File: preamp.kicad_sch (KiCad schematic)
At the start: 22 parts, among them U2 TL972QDRQ1

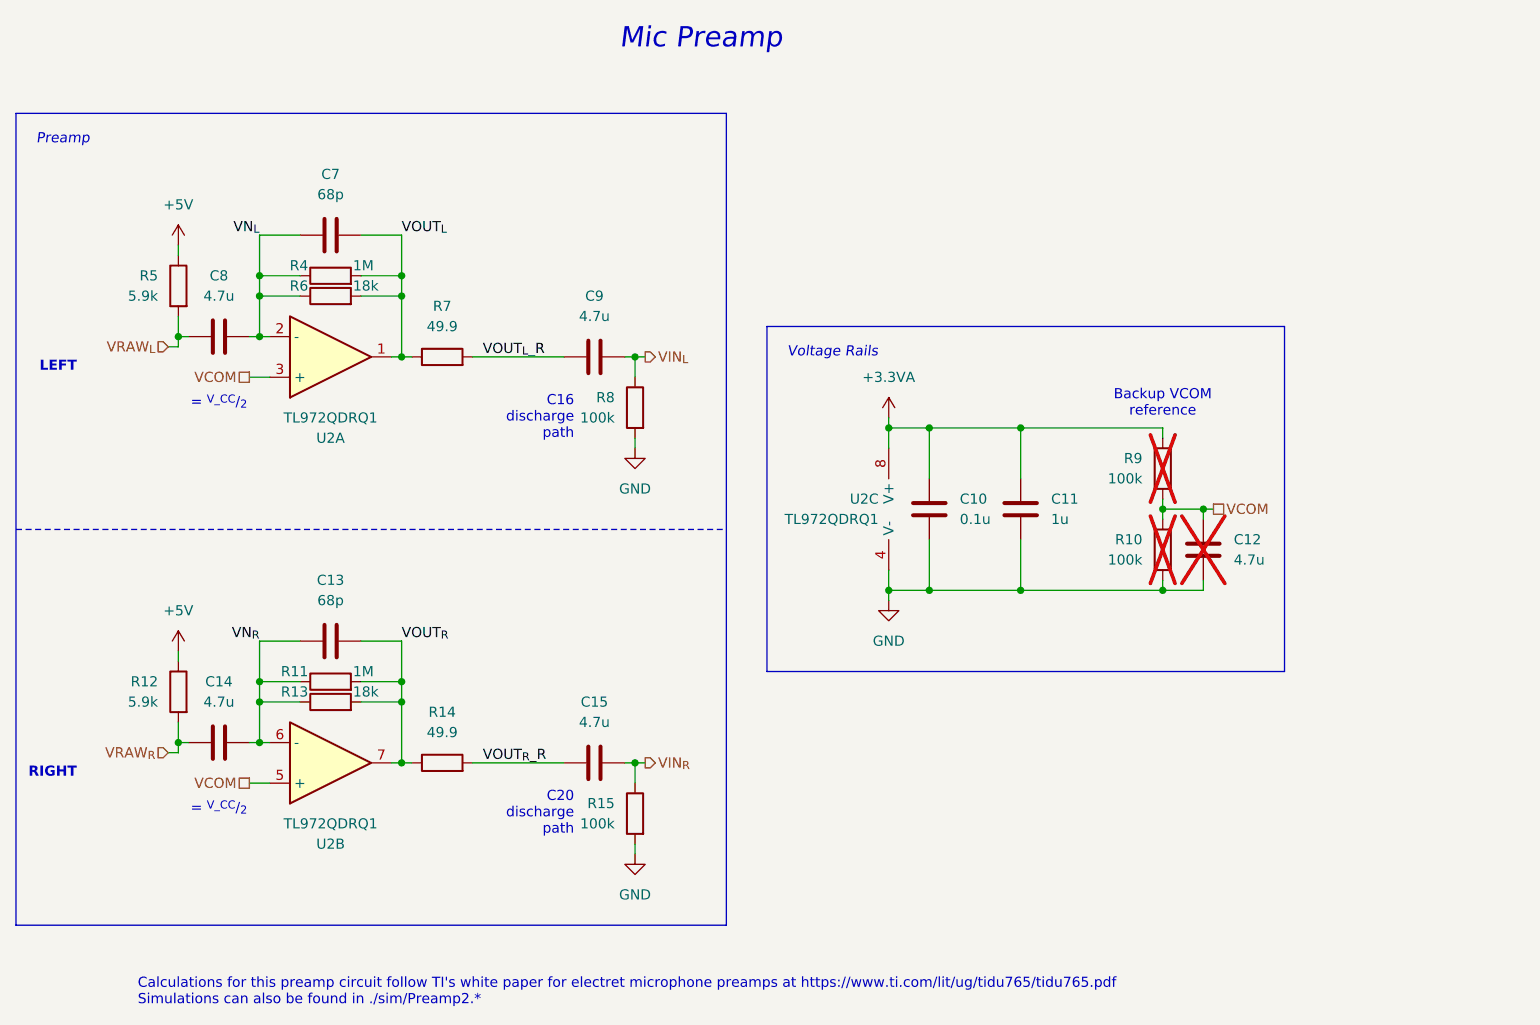
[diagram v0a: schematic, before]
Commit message: Redid schematic and component values according to new recalculations
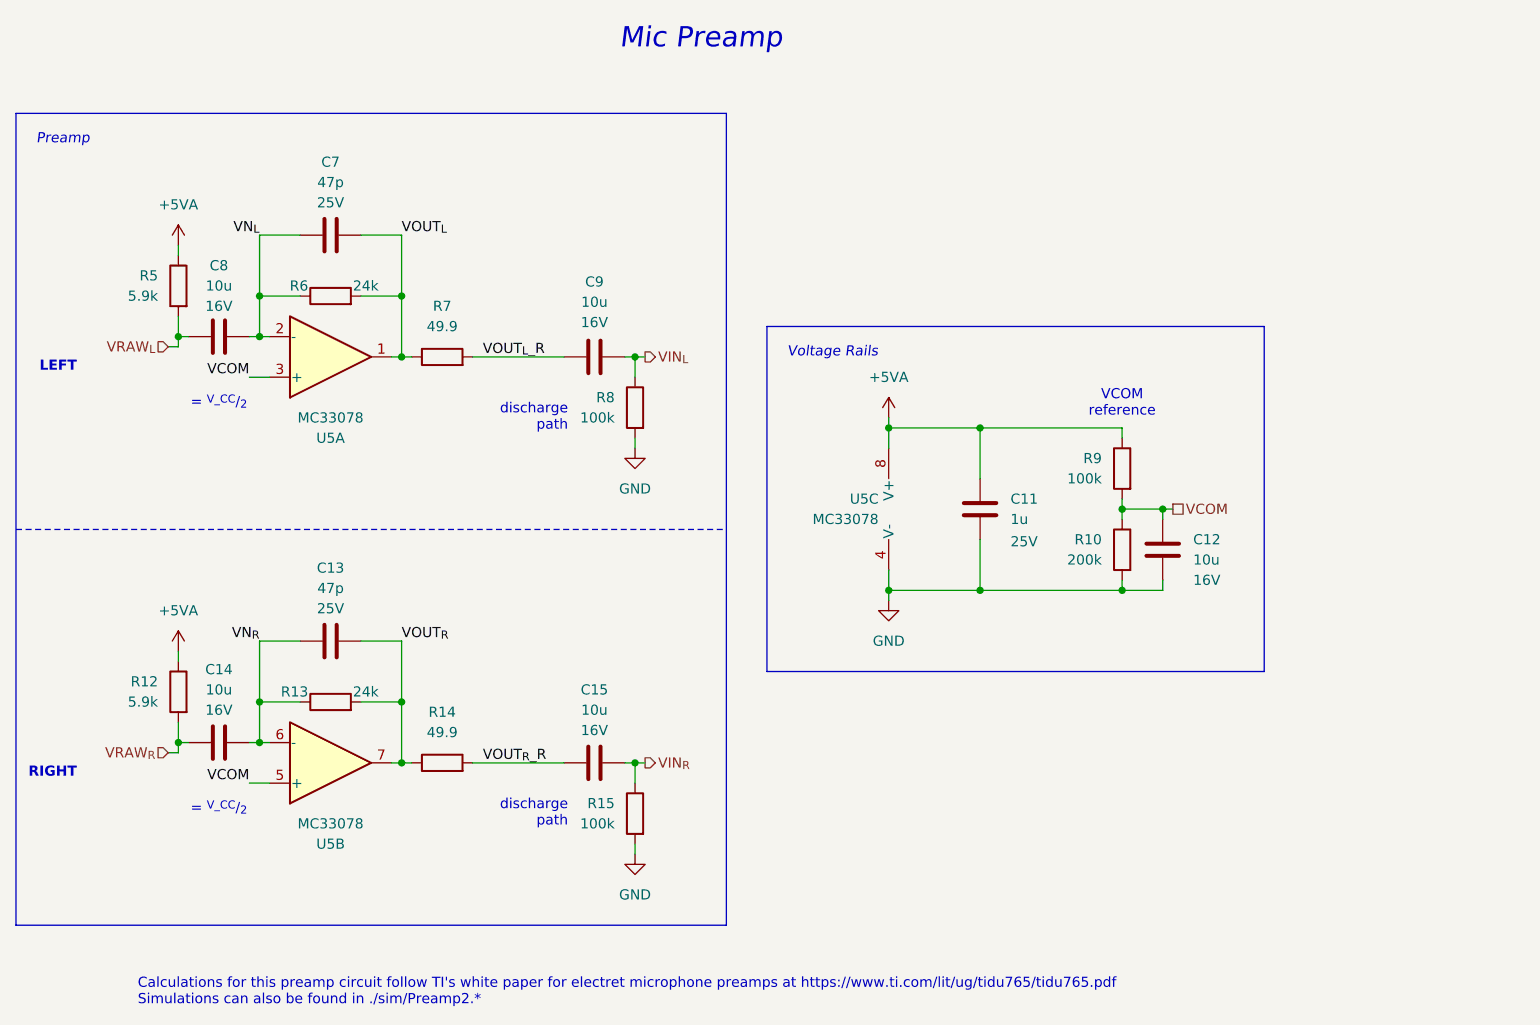
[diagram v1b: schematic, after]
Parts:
- removed C10: 0.1u, Capacitor_SMD:C_0805_2012Metric_Pad1.18x1.45mm_HandSolder, symbol Device:C
- removed R11, R4: 1M, Resistor_SMD:R_0603_1608Metric_Pad0.98x0.95mm_HandSolder, symbol Device:R
- removed U2: TL972QDRQ1, Package_SO:SOIC-8_3.9x4.9mm_P1.27mm, symbol Device:Opamp_Dual
- added U5: MC33078, Package_SO:SOIC-8_3.9x4.9mm_P1.27mm, symbol Amplifier_Operational:MC33078
- C11: footprint Capacitor_SMD:C_1206_3216Metric_Pad1.33x1.80mm_HandSolder -> Capacitor_SMD:C_0603_1608Metric_Pad1.08x0.95mm_HandSolder; Mouser Part Number 581-TAJA105K020TNJ -> 187-CL10B105KA8NNNL; Voltage Rating (none) -> 25V
- C12: value 4.7u -> 10u; Mouser Part Number 581-TAJA475K016R -> 581-TAJA106K016R; Voltage Rating (none) -> 16V; now fitted
- C13, C7: value 68p -> 47p; Mouser Part Number 77-VJ0603D680FXPAJ -> 77-VJ0603A470JXXCBC; Voltage Rating (none) -> 25V
- C14, C15, C8, C9: value 4.7u -> 10u; Mouser Part Number 581-TAJA475K016R -> 581-TAJA106K016R; Voltage Rating (none) -> 16V
- R10: value 100k -> 200k; Mouser Part Number 603-RT0603FRE10100KL -> 603-AF0603FR-07200KL; now fitted
- R13, R6: value 18k -> 24k; Mouser Part Number 667-ERA-3AEB183V -> 03-RT0603DRD0724KL
- R9: now fitted
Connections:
- net +5V is gone; now on net +5VA: R12.1, R5.1
- net GND: now also U5.4 (V-)
- net VCOM: now also U5.3 (+), U5.5 (+)
- net VN_{L}: now also U5.2 (-)
- net VN_{R}: now also U5.6 (-)
- net VOUT_{L}: now also U5.1
- net VOUT_{R}: now also U5.7
- net +3.3VA renamed +5VA
- net +5VA: now also U5.8 (V+)
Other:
- note added: "VCOM reference"
- note added: "discharge path"
- note removed: "Backup VCOM reference"
- note removed: "C16 discharge path"
- note removed: "C20 discharge path"
- moved on the sheet: C11

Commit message: Add buttons for device control + various other changes
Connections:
- net +5VA: now also R10.1; no longer R9.1
- net GND: now also R9.2; no longer R10.2
- net VCOM: now also R10.2, R9.1; no longer R10.1, R9.2
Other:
- moved on the sheet: R10, R9
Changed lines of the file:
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@@
 	(symbol
 		(lib_id "Device:R")
-		(at 207.01 91.44 0)
+		(at 207.01 101.6 0)
 		(mirror y)
 		(unit 1)
@@
 		(dnp no)
 		(property "Reference" "R9"
-			(at 204.47 90.1699 0)
+			(at 204.47 100.3299 0)
 			(effects
 				(font
@@
 		)
 		(property "Value" "100k"
-			(at 204.47 92.7099 0)
+			(at 204.47 102.8699 0)
 			(effects
 				(font
@@
 		)
 		(property "Footprint" "Resistor_SMD:R_0603_1608Metric_Pad0.98x0.95mm_HandSolder"
-			(at 208.788 91.44 90)
+			(at 208.788 101.6 90)
 			(effects
 				(font
@@
 		)
 		(property "Datasheet" "https://www.mouser.com/datasheet/2/447/PYu_RT_1_to_0_01_RoHS_L_15-3461507.pdf"
-			(at 207.01 91.44 0)
+			(at 207.01 101.6 0)
 			(effects
 				(font
@@
 		)
 		(property "Description" "Resistor"
-			(at 207.01 91.44 0)
+			(at 207.01 101.6 0)
 			(effects
 				(font
@@
 		)
 		(property "Mouser Part Number" "603-RT0603FRE10100KL"
-			(at 207.01 91.44 0)
+			(at 207.01 101.6 0)
 			(effects
 				(font
@@
 		)
 		(property "Voltage Rating" ""
-			(at 207.01 91.44 0)
+			(at 207.01 101.6 0)
 			(effects
 				(font
@@
 	(symbol
 		(lib_id "Device:R")
-		(at 207.01 101.6 0)
+		(at 207.01 91.44 0)
 		(mirror y)
 		(unit 1)
@@
 		(dnp no)
 		(property "Reference" "R10"
-			(at 204.47 100.3299 0)
+			(at 204.47 90.1699 0)
 			(effects
 				(font
@@
 		)
 		(property "Value" "200k"
-			(at 204.47 102.8699 0)
+			(at 204.47 92.7099 0)
 			(effects
 				(font
@@
 		)
 		(property "Footprint" "Resistor_SMD:R_0603_1608Metric_Pad0.98x0.95mm_HandSolder"
-			(at 208.788 101.6 90)
+			(at 208.788 91.44 90)
 			(effects
 				(font
@@
 		)
 		(property "Datasheet" "https://www.mouser.com/datasheet/2/447/PYu_AF_51_RoHS_L_9-3358811.pdf"
-			(at 207.01 101.6 0)
+			(at 207.01 91.44 0)
 			(effects
 				(font
@@
 		)
 		(property "Description" "Resistor"
-			(at 207.01 101.6 0)
+			(at 207.01 91.44 0)
 			(effects
 				(font
@@
 		)
 		(property "Mouser Part Number" "603-AF0603FR-07200KL"
-			(at 207.01 101.6 0)
+			(at 207.01 91.44 0)
 			(effects
 				(font
@@
 		)
 		(property "Voltage Rating" ""
-			(at 207.01 101.6 0)
-			(effects
-				(font
+			(at 207.01 91.44 0)
+			(effects
+				(font
